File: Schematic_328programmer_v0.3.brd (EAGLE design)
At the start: 53.9 x 54.3 mm, 15 parts, among them IC1 ATTiny85, U1 ATMEGA328P_TQFP, Y1 16mhz

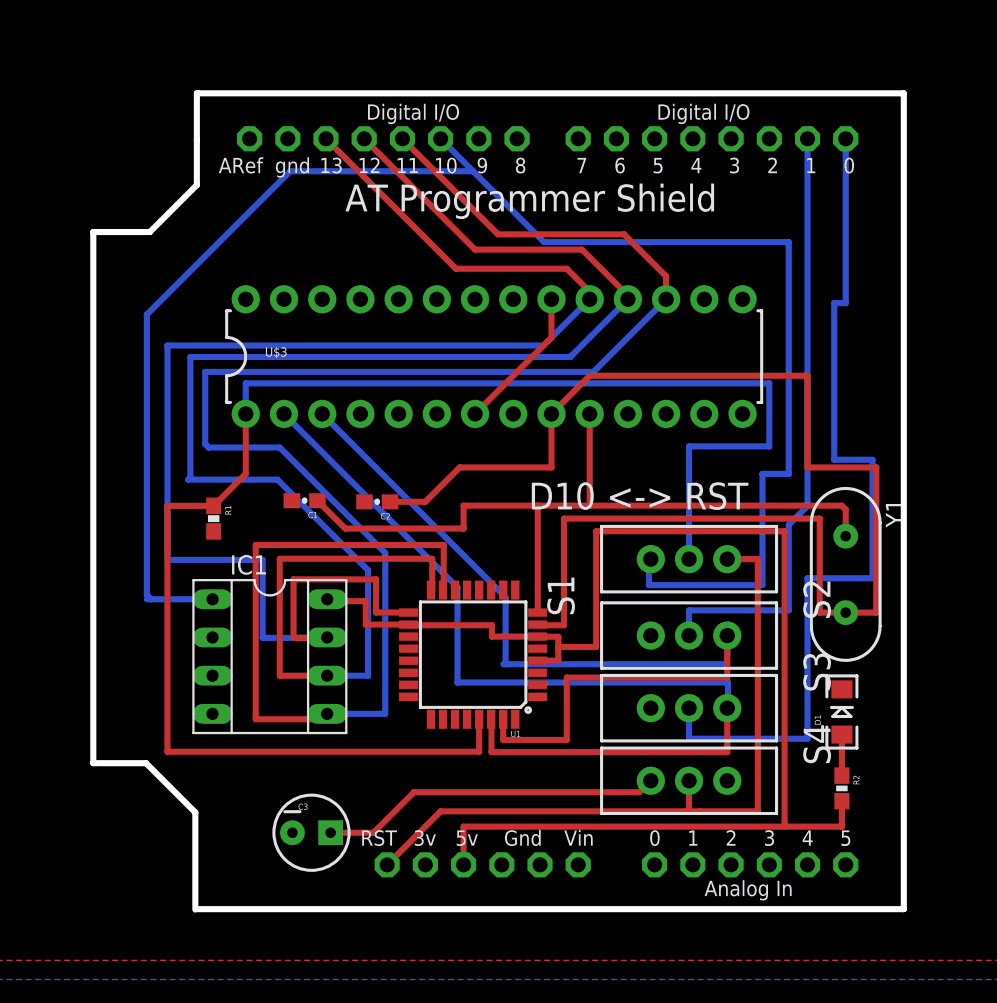
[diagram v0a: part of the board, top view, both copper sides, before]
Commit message: Updated Board CAD files
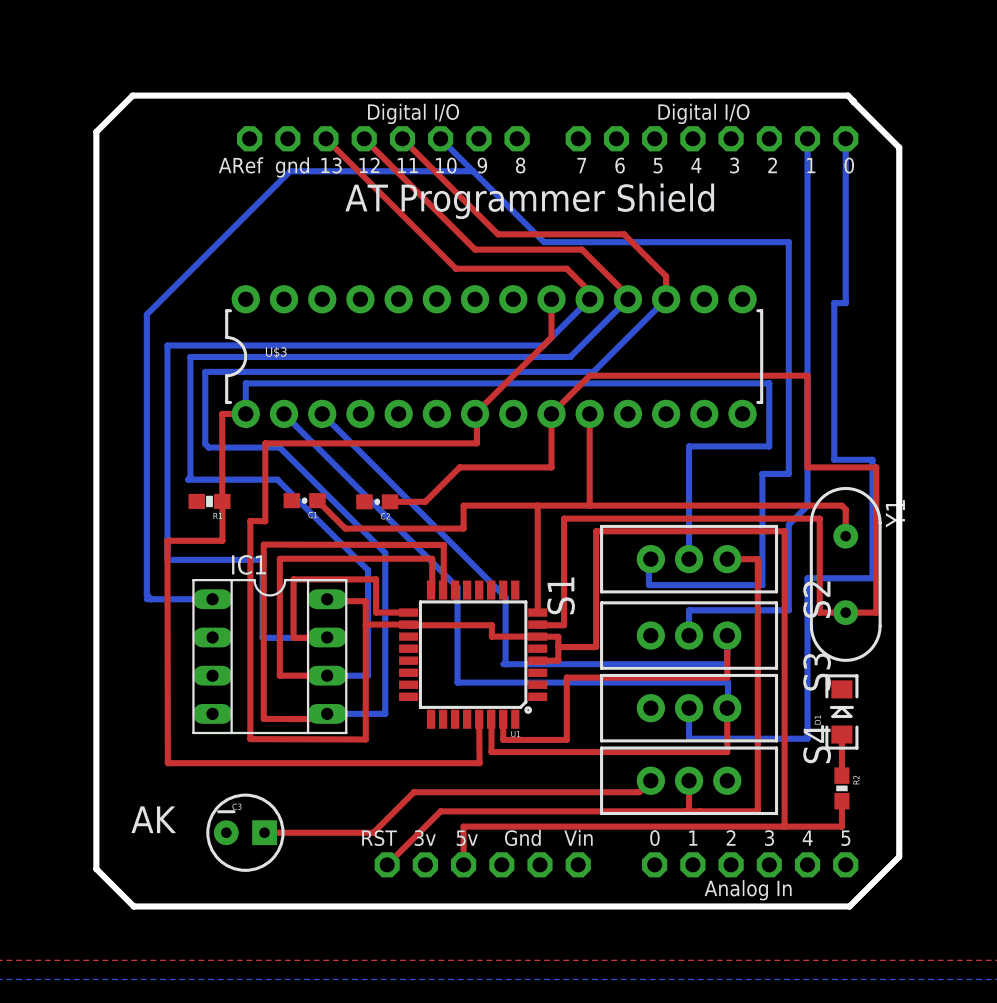
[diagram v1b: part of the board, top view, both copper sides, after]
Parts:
- moved C3 4.39 mm to (29.9, 5.94)
- moved R1 1.18 mm to (27.6, 28.0), turned to 180 degrees
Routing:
- net VCC: track 102.3 -> 154.4 mm
- net N$5: track 22.7 -> 27.1 mm
- net RESISTOR: track 103.5 -> 106.3 mm
- net D11: track 122.0 -> 120.9 mm
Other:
- board size 53.9 x 54.3 mm -> 53.4 x 53.9 mm
- board text added: "AK"
- board text removed: "D10 <-> RST"
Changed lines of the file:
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@@
 <board>
 <plain>
-<text x="48.768" y="27.432" size="1.778" layer="21">D10 &lt;-&gt; RST</text>
 <text x="36.576" y="47.244" size="1.778" layer="21">AT Programmer Shield</text>
-<wire x1="26.7716" y1="0.8636" x2="73.7108" y2="0.8636" width="0.4064" layer="20"/>
-<wire x1="73.7108" y1="0.8636" x2="73.7108" y2="55.0926" width="0.4064" layer="20"/>
-<wire x1="73.7108" y1="55.0926" x2="26.8478" y2="55.0926" width="0.4064" layer="20"/>
-<wire x1="26.6192" y1="0.8382" x2="26.6192" y2="7.2898" width="0.4064" layer="20"/>
-<wire x1="26.6192" y1="7.2898" x2="23.3426" y2="10.5664" width="0.4064" layer="20"/>
-<wire x1="23.3426" y1="10.5664" x2="19.8374" y2="10.5664" width="0.4064" layer="20"/>
-<wire x1="19.8374" y1="10.5664" x2="19.8374" y2="45.8724" width="0.4064" layer="20"/>
-<wire x1="19.8374" y1="45.8724" x2="23.5966" y2="45.8724" width="0.4064" layer="20"/>
-<wire x1="23.5966" y1="45.8724" x2="26.7208" y2="48.9966" width="0.4064" layer="20"/>
-<wire x1="26.7208" y1="48.9966" x2="26.7208" y2="51.943" width="0.4064" layer="20"/>
-<wire x1="26.7208" y1="51.943" x2="26.7208" y2="51.9684" width="0.4064" layer="20"/>
-<wire x1="26.797" y1="55.0926" x2="26.7208" y2="55.0926" width="0.4064" layer="20"/>
-<wire x1="26.7208" y1="55.0926" x2="26.7208" y2="51.9684" width="0.4064" layer="20"/>
+<wire x1="70.2818" y1="54.61" x2="70.3834" y2="54.5084" width="0.4064" layer="20"/>
+<wire x1="70.3834" y1="54.5084" x2="73.406" y2="51.4858" width="0.4064" layer="20"/>
+<wire x1="73.406" y1="51.4858" x2="73.406" y2="4.3434" width="0.4064" layer="20"/>
+<wire x1="73.406" y1="4.3434" x2="70.104" y2="1.0414" width="0.4064" layer="20"/>
+<wire x1="70.104" y1="1.0414" x2="22.5298" y2="1.0414" width="0.4064" layer="20"/>
+<wire x1="22.5298" y1="1.0414" x2="20.0406" y2="3.5306" width="0.4064" layer="20"/>
+<wire x1="20.0406" y1="3.5306" x2="20.0406" y2="52.5272" width="0.4064" layer="20"/>
+<wire x1="20.0406" y1="52.5272" x2="22.4536" y2="54.9402" width="0.4064" layer="20"/>
+<wire x1="22.4536" y1="54.9402" x2="70.0024" y2="54.9402" width="0.4064" layer="20"/>
+<wire x1="70.0024" y1="54.9402" x2="70.3834" y2="54.5592" width="0.4064" layer="20"/>
+<wire x1="70.3834" y1="54.5592" x2="70.3834" y2="54.5084" width="0.4064" layer="20"/>
+<text x="22.352" y="5.9182" size="1.778" layer="21" font="vector">AK</text>
 </plain>
 <attributes>
@@
 <attribute name="PROD_ID" value="DIO-09911" x="69.596" y="13.97" size="1.778" layer="27" rot="R90" display="off"/>
 </element>
-<element name="R1" library="SparkFun-Passives" package="0603-RES" value="10k" x="27.8384" y="26.8224" rot="R270"/>
+<element name="R1" library="SparkFun-Passives" package="0603-RES" value="10k" x="27.559" y="27.9654" rot="R180"/>
 <element name="R2" library="SparkFun-Resistors" package="0603-RES" value="220 ohm" x="69.596" y="8.89" rot="R270"/>
 <element name="S1" library="SparkFun-Electromechanical" package="SWITCH-SPDT" value="bootloader vs programmer " x="59.436" y="24.13" rot="R90">
@@
 <attribute name="PROD_ID" value="SWCH-08261" x="59.436" y="9.398" size="1.778" layer="27" rot="R270" display="off"/>
 </element>
-<element name="C3" library="SparkFun-Capacitors" package="CPOL-RADIAL-10UF-25V" value="10uF" x="34.3408" y="5.9436">
-<attribute name="PROD_ID" value="CAP-08440" x="34.3408" y="5.9436" size="1.778" layer="27" display="off"/>
+<element name="C3" library="SparkFun-Capacitors" package="CPOL-RADIAL-10UF-25V" value="10uF" x="29.9466" y="5.9436">
+<attribute name="PROD_ID" value="CAP-08440" x="29.9466" y="5.9436" size="1.778" layer="27" display="off"/>
 </element>
 </elements>
@@
 <wire x1="64.77" y1="31.623" x2="59.436" y2="31.623" width="0.4064" layer="16"/>
 <wire x1="59.436" y1="31.623" x2="59.436" y2="24.13" width="0.4064" layer="16"/>
-<wire x1="27.8384" y1="27.6724" x2="29.972" y2="29.806" width="0.4064" layer="1"/>
-<wire x1="29.972" y1="29.806" x2="29.972" y2="33.782" width="0.4064" layer="1"/>
-<wire x1="45.485" y1="11.3284" x2="24.765" y2="11.3284" width="0.4064" layer="1"/>
-<wire x1="24.765" y1="11.3284" x2="24.765" y2="27.6724" width="0.4064" layer="1"/>
-<wire x1="24.765" y1="27.6724" x2="27.8384" y2="27.6724" width="0.4064" layer="1"/>
-<wire x1="45.485" y1="11.3284" x2="45.485" y2="13.4874" width="0.4064" layer="1"/>
+<wire x1="45.5104" y1="10.5664" x2="24.7904" y2="10.5664" width="0.4064" layer="1"/>
+<wire x1="45.5104" y1="10.5664" x2="45.485" y2="13.4874" width="0.4064" layer="1"/>
+<wire x1="24.7904" y1="10.5664" x2="24.765" y2="25.3492" width="0.4064" layer="1"/>
+<wire x1="24.765" y1="25.3492" x2="28.4226" y2="25.3492" width="0.4064" layer="1"/>
+<wire x1="28.4226" y1="25.3492" x2="28.4226" y2="27.9654" width="0.4064" layer="1"/>
+<wire x1="28.4226" y1="27.9654" x2="28.409" y2="27.9654" width="0.4064" layer="1"/>
+<wire x1="28.409" y1="27.9654" x2="28.409" y2="33.782" width="0.4064" layer="1"/>
+<wire x1="28.409" y1="33.782" x2="29.972" y2="33.782" width="0.4064" layer="1"/>
 </signal>
 <signal name="VCC">
@@
 <wire x1="37.9476" y1="21.336" x2="37.9476" y2="19.78" width="0.4064" layer="1"/>
 <wire x1="37.9476" y1="19.78" x2="40.7924" y2="19.78" width="0.4064" layer="1"/>
-<wire x1="53.2638" y1="25.9842" x2="45.212" y2="33.782" width="0" layer="19" extent="1-1"/>
+<wire x1="45.212" y1="33.782" x2="45.339" y2="33.782" width="0.4064" layer="1"/>
+<wire x1="45.339" y1="33.782" x2="45.339" y2="31.8262" width="0.4064" layer="1"/>
+<wire x1="45.339" y1="31.8262" x2="31.2674" y2="31.8262" width="0.4064" layer="1"/>
+<wire x1="31.2674" y1="31.8262" x2="31.2674" y2="26.6446" width="0.4064" layer="1"/>
+<wire x1="31.2674" y1="26.6446" x2="30.2768" y2="26.67" width="0.4064" layer="1"/>
+<wire x1="30.2768" y1="26.67" x2="30.2768" y2="12.1666" width="0.4064" layer="1"/>
+<wire x1="30.2768" y1="12.1666" x2="37.9476" y2="12.1412" width="0.4064" layer="1"/>
+<wire x1="37.9476" y1="12.1412" x2="37.9476" y2="19.78" width="0.4064" layer="1"/>
 </signal>
 <signal name="D13">
@@
 <wire x1="57.912" y1="41.402" x2="53.086" y2="36.576" width="0.4064" layer="16"/>
 <wire x1="35.3822" y1="13.843" x2="35.3822" y2="13.4874" width="0.4064" layer="1"/>
-<wire x1="35.3822" y1="13.4874" x2="30.6324" y2="13.4874" width="0.4064" layer="1"/>
-<wire x1="30.6324" y1="13.4874" x2="30.6324" y2="25.0698" width="0.4064" layer="1"/>
-<wire x1="30.6324" y1="25.0698" x2="43.1292" y2="25.0698" width="0.4064" layer="1"/>
+<wire x1="35.3822" y1="13.4874" x2="31.1658" y2="13.5128" width="0.4064" layer="1"/>
+<wire x1="31.1658" y1="13.5128" x2="31.1658" y2="25.0952" width="0.4064" layer="1"/>
+<wire x1="31.1658" y1="25.0952" x2="43.1292" y2="25.0698" width="0.4064" layer="1"/>
 <wire x1="43.1292" y1="25.0698" x2="43.1292" y2="22.0726" width="0.4064" layer="1"/>
 <wire x1="43.1292" y1="22.0726" x2="43.085" y2="22.0726" width="0.4064" layer="1"/>
@@
 <wire x1="56.134" y1="8.636" x2="41.148" y2="8.636" width="0.4064" layer="1"/>
 <wire x1="41.148" y1="8.636" x2="38.4556" y2="5.9436" width="0.4064" layer="1"/>
-<wire x1="38.4556" y1="5.9436" x2="35.6108" y2="5.9436" width="0.4064" layer="1"/>
+<wire x1="38.4556" y1="5.9436" x2="31.2166" y2="5.9436" width="0.4064" layer="1"/>
 </signal>
 </signals>
